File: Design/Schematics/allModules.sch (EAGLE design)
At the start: 197 parts, among them IC1 MAX7219CNG, IC2 MAX7219CNG, IC3 MAX7219CNG, IC4 MAX7219CNG, IC5 MCP3008, SW1 arcade_btn, SW2 arcade_btn, SW3 arcade_btn, SW4 arcade_btn, U1 328P, U2 328P, U3 328P, U4 328P, U5 328P, U6 328P

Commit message: Added connection betwen main module and config module
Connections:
- net ESP_RX: now also U1.PB1(OC1A)
- net ESP_TX: now also U1.PB0(ICP)
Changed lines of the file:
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@@
+</segment>
+</net>
+<net name="ESP_RX" class="0">
+<segment>
+<pinref part="U1" gate="G$1" pin="PB1(OC1A)"/>
+<wire x1="-200.66" y1="66.04" x2="-195.58" y2="66.04" width="0.1524" layer="91"/>
+<label x="-195.58" y="66.04" size="1.778" layer="95"/>
+</segment>
+</net>
+<net name="ESP_TX" class="0">
+<segment>
+<pinref part="U1" gate="G$1" pin="PB0(ICP)"/>
+<wire x1="-200.66" y1="68.58" x2="-198.12" y2="68.58" width="0.1524" layer="91"/>
+<label x="-198.12" y="68.58" size="1.778" layer="95"/>
 </segment>
 </net>

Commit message: Replace simon says buttons to switches
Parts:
- removed R10, R11, R12, R13: 10k, adafruit:R-US_0309/12
- removed SW1, SW2, SW3, SW4: arcade_btn, adafruit:SWITCH_PUSHBUTTONC&K_KSS
- added S1, S2, S3, S4: (no value), adafruit:EG1218S
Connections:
- net GND: now also S1.S, S2.S, S3.S, S4.S; no longer SW1.P$2, SW2.P$2, SW3.P$2, SW4.P$2
- net N$34: now also S4.P; no longer R10.1, SW4.P$1
- net N$35: now also S3.P; no longer R11.1, SW3.P$1
- net N$38: now also S2.P; no longer R12.1, SW1.P$1
- net N$39: now also S1.P; no longer R13.1, SW2.P$1
- net VCC: now also S1.O, S2.O, S3.O, S4.O; no longer R10.2, R11.2, R12.2, R13.2

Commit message: Renamed simon says buttons
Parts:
- removed S1, S2, S3: (no value), adafruit:EG1218S
- added GRN_BTN, RED_BTN, YEL_BTN: (no value), adafruit:EG1218S
- renumbered S4 to BLU_BTN
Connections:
- net GND: now also GRN_BTN.S, RED_BTN.S, YEL_BTN.S; no longer S1.S, S2.S, S3.S
- net N$35: now also GRN_BTN.P; no longer S3.P
- net N$38: now also YEL_BTN.P; no longer S2.P
- net N$39: now also RED_BTN.P; no longer S1.P
- net VCC: now also GRN_BTN.O, RED_BTN.O, YEL_BTN.O; no longer S1.O, S2.O, S3.O
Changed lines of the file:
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@@
 <part name="VCC27" library="m-pad-2.1" deviceset="VCC" device=""/>
 <part name="C3" library="adafruit" library_urn="urn:adsk.eagle:library:420" deviceset="C-US" device="025-024X044" package3d_urn="urn:adsk.eagle:package:6240324/1" value="100n"/>
-<part name="S1" library="adafruit" library_urn="urn:adsk.eagle:library:420" deviceset="EG1218" device="S" package3d_urn="urn:adsk.eagle:package:6240649/1"/>
-<part name="S2" library="adafruit" library_urn="urn:adsk.eagle:library:420" deviceset="EG1218" device="S" package3d_urn="urn:adsk.eagle:package:6240649/1"/>
-<part name="S3" library="adafruit" library_urn="urn:adsk.eagle:library:420" deviceset="EG1218" device="S" package3d_urn="urn:adsk.eagle:package:6240649/1"/>
-<part name="S4" library="adafruit" library_urn="urn:adsk.eagle:library:420" deviceset="EG1218" device="S" package3d_urn="urn:adsk.eagle:package:6240649/1"/>
+<part name="RED_BTN" library="adafruit" library_urn="urn:adsk.eagle:library:420" deviceset="EG1218" device="S" package3d_urn="urn:adsk.eagle:package:6240649/1"/>
+<part name="YEL_BTN" library="adafruit" library_urn="urn:adsk.eagle:library:420" deviceset="EG1218" device="S" package3d_urn="urn:adsk.eagle:package:6240649/1"/>
+<part name="GRN_BTN" library="adafruit" library_urn="urn:adsk.eagle:library:420" deviceset="EG1218" device="S" package3d_urn="urn:adsk.eagle:package:6240649/1"/>
+<part name="BLU_BTN" library="adafruit" library_urn="urn:adsk.eagle:library:420" deviceset="EG1218" device="S" package3d_urn="urn:adsk.eagle:package:6240649/1"/>
 </parts>
 <sheets>
@@
 <attribute name="VALUE" x="8.128" y="-23.495" size="1.778" layer="96"/>
 </instance>
-<instance part="SUPPLY7" gate="G$1" x="12.7" y="60.96" smashed="yes" rot="R90">
-<attribute name="VALUE" x="15.875" y="60.96" size="1.778" layer="96" rot="R90" align="center"/>
-</instance>
-<instance part="SUPPLY8" gate="G$1" x="12.7" y="48.26" smashed="yes" rot="R90">
-<attribute name="VALUE" x="15.875" y="48.26" size="1.778" layer="96" rot="R90" align="center"/>
-</instance>
-<instance part="SUPPLY9" gate="G$1" x="12.7" y="35.56" smashed="yes" rot="R90">
-<attribute name="VALUE" x="15.875" y="35.56" size="1.778" layer="96" rot="R90" align="center"/>
+<instance part="SUPPLY7" gate="G$1" x="12.7" y="68.58" smashed="yes" rot="R90">
+<attribute name="VALUE" x="15.875" y="68.58" size="1.778" layer="96" rot="R90" align="center"/>
+</instance>
+<instance part="SUPPLY8" gate="G$1" x="12.7" y="53.34" smashed="yes" rot="R90">
+<attribute name="VALUE" x="15.875" y="53.34" size="1.778" layer="96" rot="R90" align="center"/>
+</instance>
+<instance part="SUPPLY9" gate="G$1" x="12.7" y="38.1" smashed="yes" rot="R90">
+<attribute name="VALUE" x="15.875" y="38.1" size="1.778" layer="96" rot="R90" align="center"/>
 </instance>
 <instance part="SUPPLY10" gate="G$1" x="12.7" y="22.86" smashed="yes" rot="R90">
@@
 <attribute name="VALUE" x="38.735" y="-2.54" size="1.778" layer="96" rot="R90" align="center"/>
 </instance>
-<instance part="S1" gate="1" x="2.54" y="66.04" smashed="yes" rot="R270">
-<attribute name="NAME" x="0.635" y="72.39" size="1.778" layer="95"/>
-<attribute name="VALUE" x="5.715" y="69.85" size="1.778" layer="96"/>
-</instance>
-<instance part="S2" gate="1" x="2.54" y="53.34" smashed="yes" rot="R270">
-<attribute name="NAME" x="0.635" y="59.69" size="1.778" layer="95"/>
-<attribute name="VALUE" x="5.715" y="57.15" size="1.778" layer="96"/>
-</instance>
-<instance part="S3" gate="1" x="2.54" y="40.64" smashed="yes" rot="R270">
-<attribute name="NAME" x="0.635" y="46.99" size="1.778" layer="95"/>
-<attribute name="VALUE" x="5.715" y="44.45" size="1.778" layer="96"/>
-</instance>
-<instance part="S4" gate="1" x="2.54" y="27.94" smashed="yes" rot="R270">
+<instance part="RED_BTN" gate="1" x="2.54" y="73.66" smashed="yes" rot="R270">
+<attribute name="NAME" x="0.635" y="80.01" size="1.778" layer="95"/>
+<attribute name="VALUE" x="5.715" y="77.47" size="1.778" layer="96"/>
+</instance>
+<instance part="YEL_BTN" gate="1" x="2.54" y="58.42" smashed="yes" rot="R270">
+<attribute name="NAME" x="0.635" y="64.77" size="1.778" layer="95"/>
+<attribute name="VALUE" x="5.715" y="62.23" size="1.778" layer="96"/>
+</instance>
+<instance part="GRN_BTN" gate="1" x="2.54" y="43.18" smashed="yes" rot="R270">
+<attribute name="NAME" x="0.635" y="49.53" size="1.778" layer="95"/>
+<attribute name="VALUE" x="5.715" y="46.99" size="1.778" layer="96"/>
+</instance>
+<instance part="BLU_BTN" gate="1" x="2.54" y="27.94" smashed="yes" rot="R270">
 <attribute name="NAME" x="0.635" y="34.29" size="1.778" layer="95"/>
 <attribute name="VALUE" x="5.715" y="31.75" size="1.778" layer="96"/>
@@
 <pinref part="U2" gate="G$1" pin="PC3(ADC3)"/>
 <wire x1="-2.54" y1="25.4" x2="-27.94" y2="25.4" width="0.1524" layer="91"/>
-<pinref part="S4" gate="1" pin="P"/>
+<pinref part="BLU_BTN" gate="1" pin="P"/>
 </segment>
 </net>
 <net name="N$35" class="0">
 <segment>
-<wire x1="-10.16" y1="38.1" x2="-10.16" y2="27.94" width="0.1524" layer="91"/>
+<wire x1="-10.16" y1="40.64" x2="-10.16" y2="27.94" width="0.1524" layer="91"/>
 <pinref part="U2" gate="G$1" pin="PC2(ADC2)"/>
 <wire x1="-27.94" y1="27.94" x2="-10.16" y2="27.94" width="0.1524" layer="91"/>
-<pinref part="S3" gate="1" pin="P"/>
-<wire x1="-10.16" y1="38.1" x2="-2.54" y2="38.1" width="0.1524" layer="91"/>
+<pinref part="GRN_BTN" gate="1" pin="P"/>
+<wire x1="-10.16" y1="40.64" x2="-2.54" y2="40.64" width="0.1524" layer="91"/>
 </segment>
 </net>
 <net name="N$38" class="0">
 <segment>
-<wire x1="-12.7" y1="50.8" x2="-12.7" y2="30.48" width="0.1524" layer="91"/>
+<wire x1="-12.7" y1="55.88" x2="-12.7" y2="30.48" width="0.1524" layer="91"/>
 <pinref part="U2" gate="G$1" pin="PC1(ADC1)"/>
 <wire x1="-12.7" y1="30.48" x2="-27.94" y2="30.48" width="0.1524" layer="91"/>
-<pinref part="S2" gate="1" pin="P"/>
-<wire x1="-2.54" y1="50.8" x2="-12.7" y2="50.8" width="0.1524" layer="91"/>
+<pinref part="YEL_BTN" gate="1" pin="P"/>
+<wire x1="-2.54" y1="55.88" x2="-12.7" y2="55.88" width="0.1524" layer="91"/>
 </segment>
 </net>
 <net name="N$39" class="0">
 <segment>
-<wire x1="-15.24" y1="33.02" x2="-15.24" y2="63.5" width="0.1524" layer="91"/>
-<wire x1="-15.24" y1="63.5" x2="-2.54" y2="63.5" width="0.1524" layer="91"/>
+<wire x1="-15.24" y1="33.02" x2="-15.24" y2="71.12" width="0.1524" layer="91"/>
+<wire x1="-15.24" y1="71.12" x2="-2.54" y2="71.12" width="0.1524" layer="91"/>
 <pinref part="U2" gate="G$1" pin="PC0(ADC0)"/>
 <wire x1="-27.94" y1="33.02" x2="-15.24" y2="33.02" width="0.1524" layer="91"/>
-<pinref part="S1" gate="1" pin="P"/>
+<pinref part="RED_BTN" gate="1" pin="P"/>
 </segment>
 </net>
@@
 </segment>
 <segment>
-<wire x1="20.32" y1="66.04" x2="20.32" y2="53.34" width="0.1524" layer="91"/>
+<wire x1="20.32" y1="73.66" x2="20.32" y2="58.42" width="0.1524" layer="91"/>
 <pinref part="VCC17" gate="1" pin="VCC"/>
-<pinref part="S1" gate="1" pin="O"/>
-<wire x1="20.32" y1="53.34" x2="20.32" y2="40.64" width="0.1524" layer="91"/>
-<wire x1="20.32" y1="40.64" x2="20.32" y2="27.94" width="0.1524" layer="91"/>
+<pinref part="RED_BTN" gate="1" pin="O"/>
+<wire x1="20.32" y1="58.42" x2="20.32" y2="43.18" width="0.1524" layer="91"/>
+<wire x1="20.32" y1="43.18" x2="20.32" y2="27.94" width="0.1524" layer="91"/>
 <wire x1="20.32" y1="27.94" x2="20.32" y2="22.86" width="0.1524" layer="91"/>
-<wire x1="7.62" y1="66.04" x2="20.32" y2="66.04" width="0.1524" layer="91"/>
-<pinref part="S2" gate="1" pin="O"/>
-<wire x1="7.62" y1="53.34" x2="20.32" y2="53.34" width="0.1524" layer="91"/>
-<junction x="20.32" y="53.34"/>
-<pinref part="S3" gate="1" pin="O"/>
-<wire x1="7.62" y1="40.64" x2="20.32" y2="40.64" width="0.1524" layer="91"/>
-<junction x="20.32" y="40.64"/>
-<pinref part="S4" gate="1" pin="O"/>
+<wire x1="7.62" y1="73.66" x2="20.32" y2="73.66" width="0.1524" layer="91"/>
+<pinref part="YEL_BTN" gate="1" pin="O"/>
+<wire x1="7.62" y1="58.42" x2="20.32" y2="58.42" width="0.1524" layer="91"/>
+<junction x="20.32" y="58.42"/>
+<pinref part="GRN_BTN" gate="1" pin="O"/>
+<wire x1="7.62" y1="43.18" x2="20.32" y2="43.18" width="0.1524" layer="91"/>
+<junction x="20.32" y="43.18"/>
+<pinref part="BLU_BTN" gate="1" pin="O"/>
 <wire x1="7.62" y1="27.94" x2="20.32" y2="27.94" width="0.1524" layer="91"/>
 <junction x="20.32" y="27.94"/>
@@
 </segment>
 <segment>
-<pinref part="S1" gate="1" pin="S"/>
+<pinref part="RED_BTN" gate="1" pin="S"/>
 <pinref part="SUPPLY7" gate="G$1" pin="GND"/>
-<wire x1="7.62" y1="60.96" x2="10.16" y2="60.96" width="0.1524" layer="91"/>
-</segment>
-<segment>
-<pinref part="S2" gate="1" pin="S"/>
+<wire x1="7.62" y1="68.58" x2="10.16" y2="68.58" width="0.1524" layer="91"/>
+</segment>
+<segment>
+<pinref part="YEL_BTN" gate="1" pin="S"/>
 <pinref part="SUPPLY8" gate="G$1" pin="GND"/>
-<wire x1="7.62" y1="48.26" x2="10.16" y2="48.26" width="0.1524" layer="91"/>
-</segment>
-<segment>
-<pinref part="S3" gate="1" pin="S"/>
+<wire x1="7.62" y1="53.34" x2="10.16" y2="53.34" width="0.1524" layer="91"/>
+</segment>
+<segment>
+<pinref part="GRN_BTN" gate="1" pin="S"/>
 <pinref part="SUPPLY9" gate="G$1" pin="GND"/>
-<wire x1="7.62" y1="35.56" x2="10.16" y2="35.56" width="0.1524" layer="91"/>
-</segment>
-<segment>
-<pinref part="S4" gate="1" pin="S"/>
+<wire x1="7.62" y1="38.1" x2="10.16" y2="38.1" width="0.1524" layer="91"/>
+</segment>
+<segment>
+<pinref part="BLU_BTN" gate="1" pin="S"/>
 <pinref part="SUPPLY10" gate="G$1" pin="GND"/>
 <wire x1="7.62" y1="22.86" x2="10.16" y2="22.86" width="0.1524" layer="91"/>

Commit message: Swapped 2 pins on MAX6954 IC for readability
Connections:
- removed net O7: MAX6954.O7
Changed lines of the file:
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@@
 <?xml version="1.0" encoding="utf-8"?>
 <!DOCTYPE eagle SYSTEM "eagle.dtd">
-<eagle version="9.6.1">
+<eagle version="9.6.2">
 <drawing>
 <settings>
@@
 </segment>
 </net>
-<net name="O7" class="0">
-<segment>
-<wire x1="-149.86" y1="119.38" x2="-149.86" y2="116.84" width="0.1524" layer="91"/>
-<pinref part="MAX6954" gate="G$1" pin="O7"/>
-<label x="-149.86" y="119.38" size="1.778" layer="95" rot="R90"/>
-</segment>
-</net>
 <net name="O8" class="0">
 <segment>
@@
 <net name="SERIAL_CLK" class="0">
 <segment>
-<pinref part="MAX6954" gate="G$1" pin="CLK"/>
-<wire x1="-144.78" y1="86.36" x2="-144.78" y2="83.82" width="0.1524" layer="91"/>
-<label x="-144.78" y="83.82" size="1.778" layer="95" rot="R270"/>
-</segment>
-<segment>
 <pinref part="U1" gate="G$1" pin="PC2(ADC2)"/>
 <wire x1="-200.66" y1="109.22" x2="-193.04" y2="109.22" width="0.1524" layer="91"/>
 <label x="-193.04" y="109.22" size="1.778" layer="95" rot="R90"/>
 </segment>
-</net>
-<net name="SERIAL_DIN" class="0">
-<segment>
-<pinref part="MAX6954" gate="G$1" pin="DIN"/>
+<segment>
+<pinref part="MAX6954" gate="G$1" pin="CLK"/>
 <wire x1="-142.24" y1="86.36" x2="-142.24" y2="83.82" width="0.1524" layer="91"/>
 <label x="-142.24" y="83.82" size="1.778" layer="95" rot="R270"/>
 </segment>
+</net>
+<net name="SERIAL_DIN" class="0">
 <segment>
 <pinref part="U1" gate="G$1" pin="PC1(ADC1)"/>
@@
 <label x="-195.58" y="111.76" size="1.778" layer="95" rot="R90"/>
 </segment>
-</net>
+<segment>
+<pinref part="MAX6954" gate="G$1" pin="DIN"/>
+<wire x1="-144.78" y1="86.36" x2="-144.78" y2="83.82" width="0.1524" layer="91"/>
+<label x="-144.78" y="83.82" size="1.778" layer="95" rot="R270"/>
+</segment>
+</net>

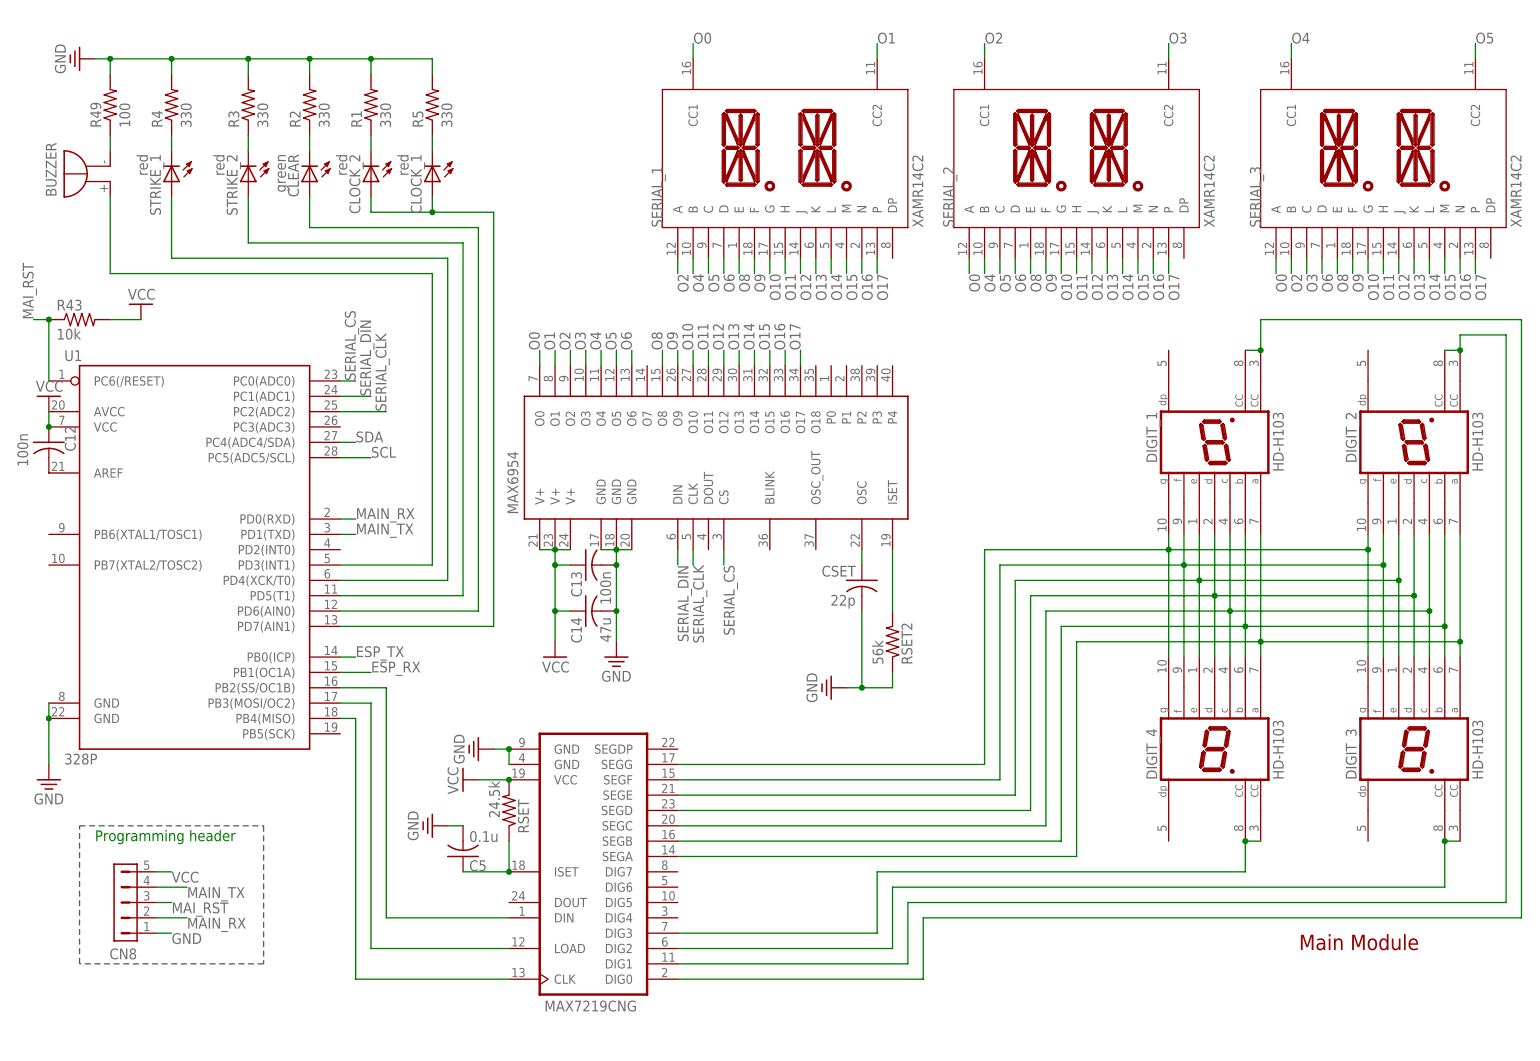
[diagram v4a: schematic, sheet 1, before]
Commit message: Added MCP23017 to schematic
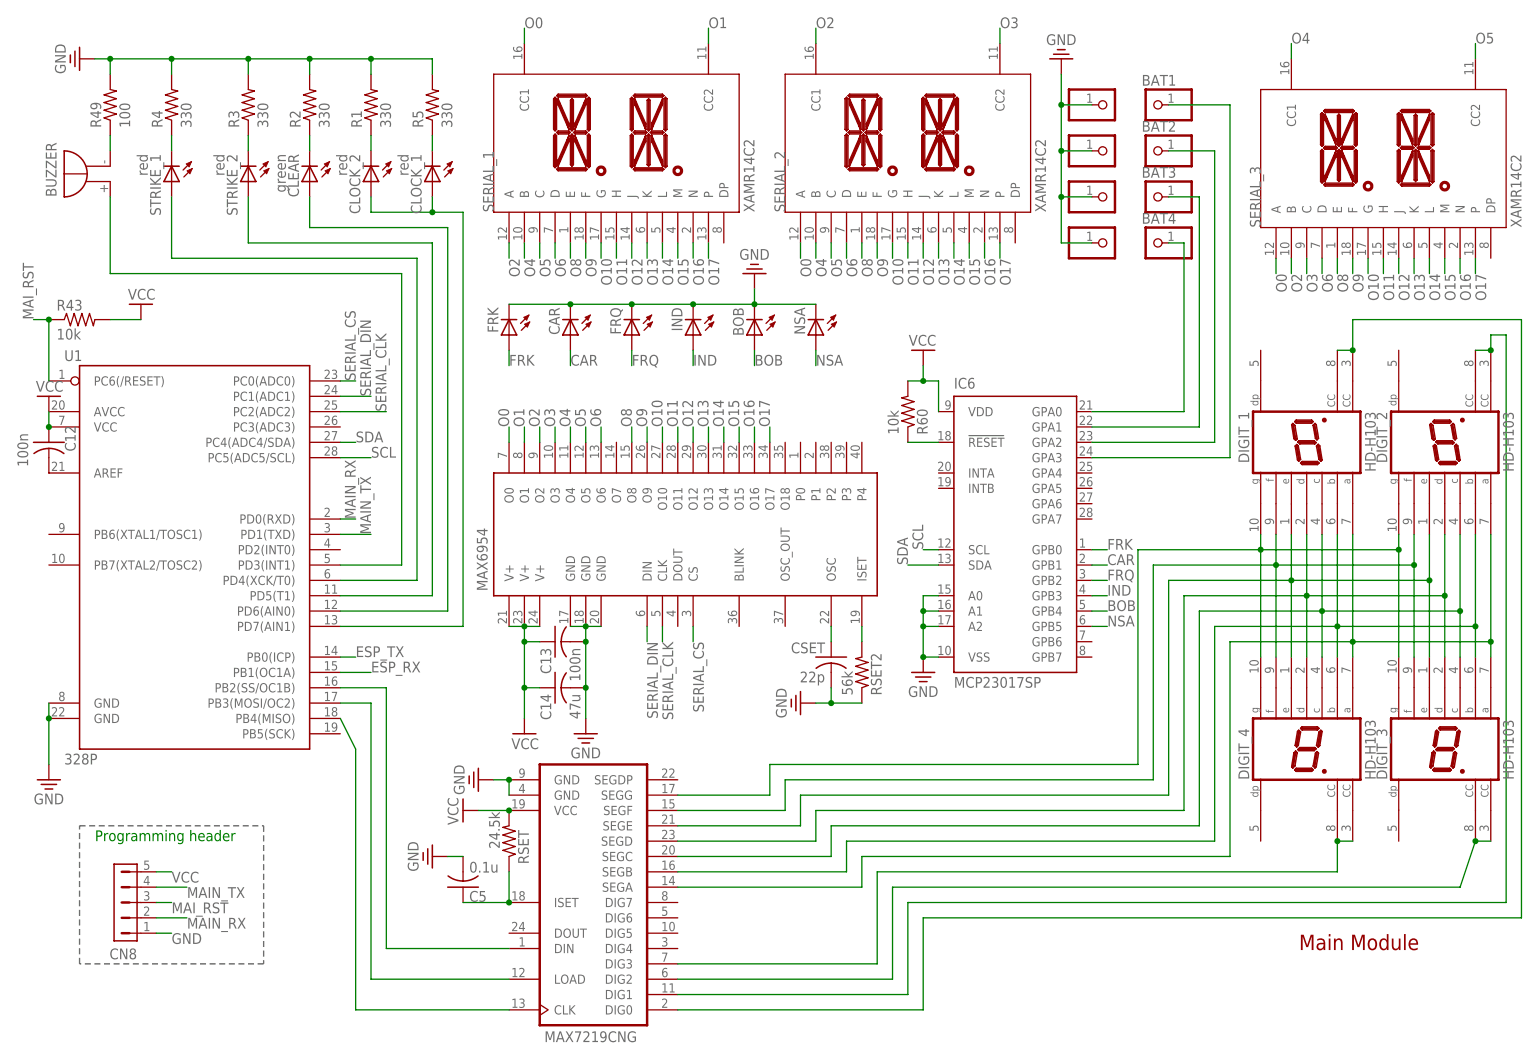
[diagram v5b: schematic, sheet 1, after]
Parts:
- added BAT1, BAT2, BAT3, BAT4, JP17, JP18, JP19, JP20: (no value), adafruit:PINHD-1X1
- added BOB, CAR, FRK, FRQ, IND, NSA: (no value), adafruit:LED5MM
- added IC6: MCP23017SP, adafruit:MCP23017SP
- added R60: 10k, BeagleBone_Black_Wireless:R-US_0204/7
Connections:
- new net BAT1: BAT1.1, IC6.GPA3
- new net BOB: BOB.A, IC6.GPB4
- new net CAR: CAR.A, IC6.GPB1
- new net FRK: FRK.A, IC6.GPB0
- new net FRQ: FRQ.A, IC6.GPB2
- new net IND: IC6.GPB3, IND.A
- new net N$108: IC6.!RESET, R60.1
- new net N$128: BAT2.1, IC6.GPA2
- new net N$141: BAT3.1, IC6.GPA1
- new net N$142: BAT4.1, IC6.GPA0
- new net NSA: IC6.GPB5, NSA.A
- net GND: now also BOB.C, CAR.C, FRK.C, FRQ.C, IC6.A0, IC6.A1, IC6.A2, IC6.VSS, IND.C, JP17.1, JP18.1, JP19.1, JP20.1, NSA.C
- net SCL: now also IC6.SCL
- net SDA: now also IC6.SDA
- net VCC: now also IC6.VDD, R60.2
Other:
- moved on the sheet: C13, C14, C5, CSET, DIGIT_1, DIGIT_2, DIGIT_3, DIGIT_4, MAX6954, RSET, RSET2, SERIAL_1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
